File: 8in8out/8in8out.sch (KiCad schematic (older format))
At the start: 58 parts, among them IC1 ATTINY48-A, J1 RJ45, J2 RJ45, J3 CONN_6, K110 G5T-1-12VDC, K120 G5T-1-12VDC, K130 G5T-1-12VDC, K140 G5T-1-12VDC, K150 G5T-1-12VDC, K160 G5T-1-12VDC, K170 G5T-1-12VDC, K180 G5T-1-12VDC, P1 CONN_5, P100 CONN_2, P101 CONN_2, P102 CONN_2, P103 CONN_2, P105 CONN_2, P106 CONN_2, P110 CONN_2, P120 CONN_2, P130 CONN_2, P140 CONN_2, P150 CONN_2, P160 CONN_2, P170 CONN_2, P180 CONN_2, P2 CONN_5, P3 CONN_10X2, P4 CONN_2, U1 7805, U10 OPTO-TRANSISTOR, U2 ULN2803, U20 OPTO-TRANSISTOR, U30 OPTO-TRANSISTOR, U40 OPTO-TRANSISTOR, U50 OPTO-TRANSISTOR, U60 OPTO-TRANSISTOR, U70 OPTO-TRANSISTOR, U80 OPTO-TRANSISTOR

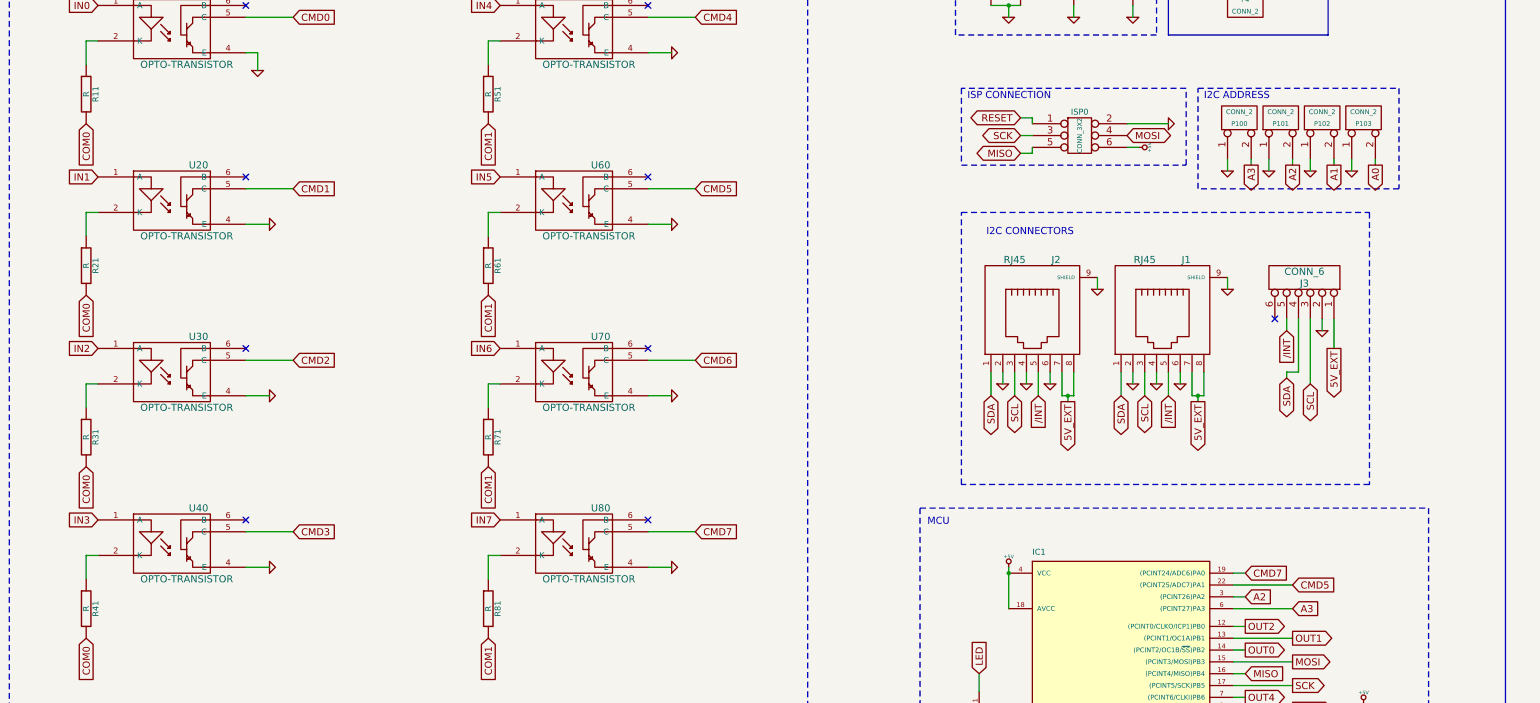
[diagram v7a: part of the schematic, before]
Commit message: reprise plan de masse pour distances de s?cu ajout r?sistances de pullup i2c doublement pistes de puissance 230VAC
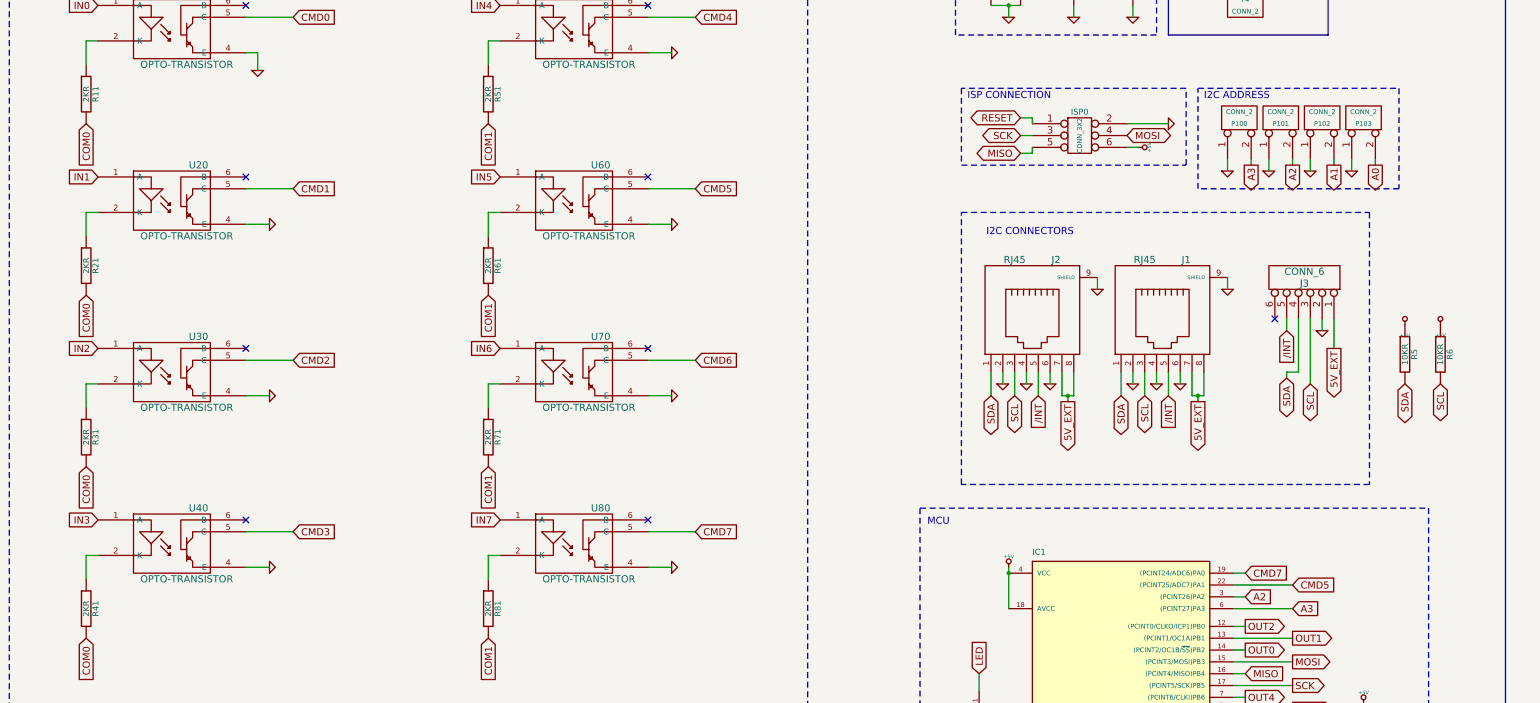
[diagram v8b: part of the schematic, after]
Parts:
- added R5, R6: 10KR, symbol R
- R11, R21, R31, R41, R51, R61, R71, R81: value R -> 2KR
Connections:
- net +5V: now also R5.1, R6.1
- net SCL: now also R6.2
- net SDA: now also R5.2
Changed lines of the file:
@@
-EESchema Schematic File Version 2  date mer. 10 avril 2013 14:01:30 CEST
+EESchema Schematic File Version 2  date mer. 10 avril 2013 22:05:12 CEST
 LIBS:g5la-1-12vdc
 LIBS:power
@@
 P 2900 4600
 F 0 "R11" V 2980 4600 50  0000 C CNN
-F 1 "R" V 2900 4600 50  0000 C CNN
+F 1 "2KR" V 2900 4600 50  0000 C CNN
 F 2 "" H 2900 4600 60  0001 C CNN
 F 3 "" H 2900 4600 60  0001 C CNN
@@
 P 2900 6050
 F 0 "R21" V 2980 6050 50  0000 C CNN
-F 1 "R" V 2900 6050 50  0000 C CNN
+F 1 "2KR" V 2900 6050 50  0000 C CNN
 F 2 "" H 2900 6050 60  0001 C CNN
 F 3 "" H 2900 6050 60  0001 C CNN
@@
 P 2900 7500
 F 0 "R31" V 2980 7500 50  0000 C CNN
-F 1 "R" V 2900 7500 50  0000 C CNN
+F 1 "2KR" V 2900 7500 50  0000 C CNN
 F 2 "" H 2900 7500 60  0001 C CNN
 F 3 "" H 2900 7500 60  0001 C CNN
@@
 P 2900 8950
 F 0 "R41" V 2980 8950 50  0000 C CNN
-F 1 "R" V 2900 8950 50  0000 C CNN
+F 1 "2KR" V 2900 8950 50  0000 C CNN
 F 2 "" H 2900 8950 60  0001 C CNN
 F 3 "" H 2900 8950 60  0001 C CNN
@@
 P 6300 4600
 F 0 "R51" V 6380 4600 50  0000 C CNN
-F 1 "R" V 6300 4600 50  0000 C CNN
+F 1 "2KR" V 6300 4600 50  0000 C CNN
 F 2 "" H 6300 4600 60  0001 C CNN
 F 3 "" H 6300 4600 60  0001 C CNN
@@
 P 6300 6050
 F 0 "R61" V 6380 6050 50  0000 C CNN
-F 1 "R" V 6300 6050 50  0000 C CNN
+F 1 "2KR" V 6300 6050 50  0000 C CNN
 F 2 "" H 6300 6050 60  0001 C CNN
 F 3 "" H 6300 6050 60  0001 C CNN
@@
 P 6300 7500
 F 0 "R71" V 6380 7500 50  0000 C CNN
-F 1 "R" V 6300 7500 50  0000 C CNN
+F 1 "2KR" V 6300 7500 50  0000 C CNN
 F 2 "" H 6300 7500 60  0001 C CNN
 F 3 "" H 6300 7500 60  0001 C CNN
@@
 P 6300 8950
 F 0 "R81" V 6380 8950 50  0000 C CNN
-F 1 "R" V 6300 8950 50  0000 C CNN
+F 1 "2KR" V 6300 8950 50  0000 C CNN
 F 2 "" H 6300 8950 60  0001 C CNN
 F 3 "" H 6300 8950 60  0001 C CNN
@@
 Text Notes 10100 12800 0    60   ~ 0
 EXTERNAL CONNECTOR (extension)
+$Comp
+L R R5
+U 1 1 5165BE3E
+P 14050 6800
+F 0 "R5" V 14130 6800 50  0000 C CNN
+F 1 "10KR" V 14050 6800 50  0000 C CNN
+F 2 "" H 14050 6800 60  0001 C CNN
+F 3 "" H 14050 6800 60  0001 C CNN
+	1    14050 6800
+	1    0    0    -1
+$EndComp
+$Comp
+L R R6
+U 1 1 5165BE57
+P 14350 6800
+F 0 "R6" V 14430 6800 50  0000 C CNN
+F 1 "10KR" V 14350 6800 50  0000 C CNN
+F 2 "" H 14350 6800 60  0001 C CNN
+F 3 "" H 14350 6800 60  0001 C CNN
+	1    14350 6800
+	1    0    0    -1
+$EndComp
+Text GLabel 14050 7050 3    60   BiDi ~ 0
+SDA
+Text GLabel 14350 7050 3    60   BiDi ~ 0
+SCL
+$Comp
+L +5V #PWR061
+U 1 1 5165C1A4
+P 14050 6550
+F 0 "#PWR061" H 14050 6460 20  0001 C CNN
+F 1 "+5V" H 14050 6460 30  0000 C CNN
+F 2 "" H 14050 6550 60  0000 C CNN
+F 3 "" H 14050 6550 60  0000 C CNN
+	1    14050 6550
+	1    0    0    -1
+$EndComp
+$Comp
+L +5V #PWR062
+U 1 1 5165C1B1
+P 14350 6550
+F 0 "#PWR062" H 14350 6460 20  0001 C CNN
+F 1 "+5V" H 14350 6460 30  0000 C CNN
+F 2 "" H 14350 6550 60  0000 C CNN
+F 3 "" H 14350 6550 60  0000 C CNN
+	1    14350 6550
+	1    0    0    -1
+$EndComp
 $EndSCHEMATC
